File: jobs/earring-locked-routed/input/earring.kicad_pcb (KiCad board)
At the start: 4 copper layers, 30.5 x 35.8 mm, 167 parts, among them J1 USB-C, Q1 ALS-PT19, Q10 BSS138W, Q2 CJ2101, Q3 BSS138W, Q4 LBSS84WT1G, Q5 BSS138W, Q6 BSS138W, Q7 BSS138W, Q8 CJ2101, Q9 BSS138W, SW2 PWR, U1 RP2350A, U10 TPS22913, U2 LGS4056H, U3 NCP730-3.3, U4 TPS22913, U5 USBLC6-2P6, U6 LSM6DS3TR-C, U7 W25Q16JVUXIQ, U8 74LVC2G14, U9 TPS22913, Y1 12MHz

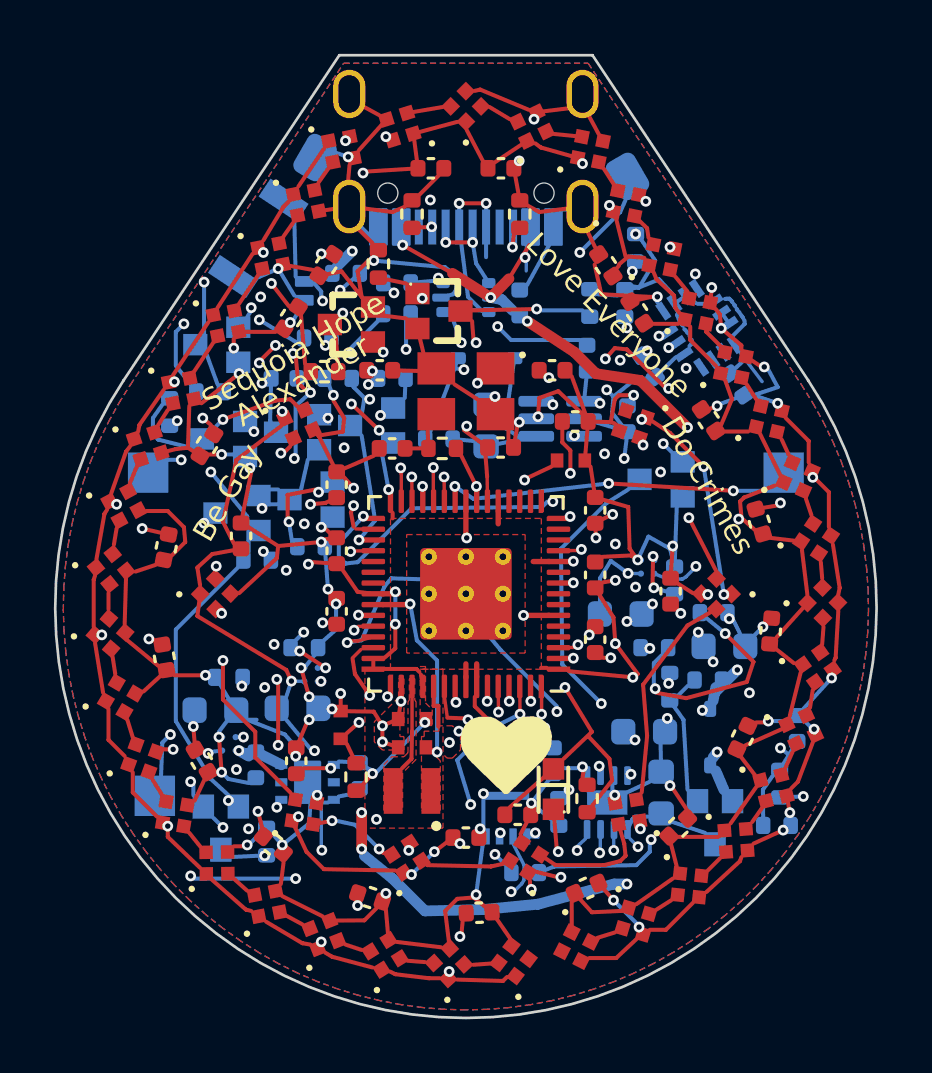
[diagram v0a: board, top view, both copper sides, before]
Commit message: Core: differential pairs routed coupled; both boards re-solved with their USB pairs
--diff-pairs finds pairs by net name (USB_DP/USB_DM, USB_C_DP/USB_C_DN, CLK_P/CLK_N, A+/A-),
takes a pad of each net close together as a pair's end, and routes each run between ends as one
centreline, wide enough for both tracks and the class's diff-pair gap, on a single layer; the
two tracks are laid along it and the router adds the pad legs. Runs go after the fine-pitch
escapes, so they block no pins, and are kept apart from copper the router may rip or pull.
The studio turns it on by default ("Route USB pairs side by side").

The cleanup cuts a track loose at both ends back to its outermost joints and cuts a tail back
to a joint already inside it, so no pair run is left dangling.

Re-solved (KiCad: 0 unconnected, 0 errors): earring-routed with USB_DP/DM 86%/78% coupled,
earring-locked-routed 92%/79%, bluebuzz-routed USB_DP/DM 81%/80% with 0.18 mm skew (the
hand-routed board: 31%). From bare pads, one thread: earring 5 of 6 seeds connected (was 4),
bluebuzz 6 of 6. examples/pair_check measures coupling.

Co-Authored-By: Claude Opus 5.5 (1M context) <noreply@anthropic.com>
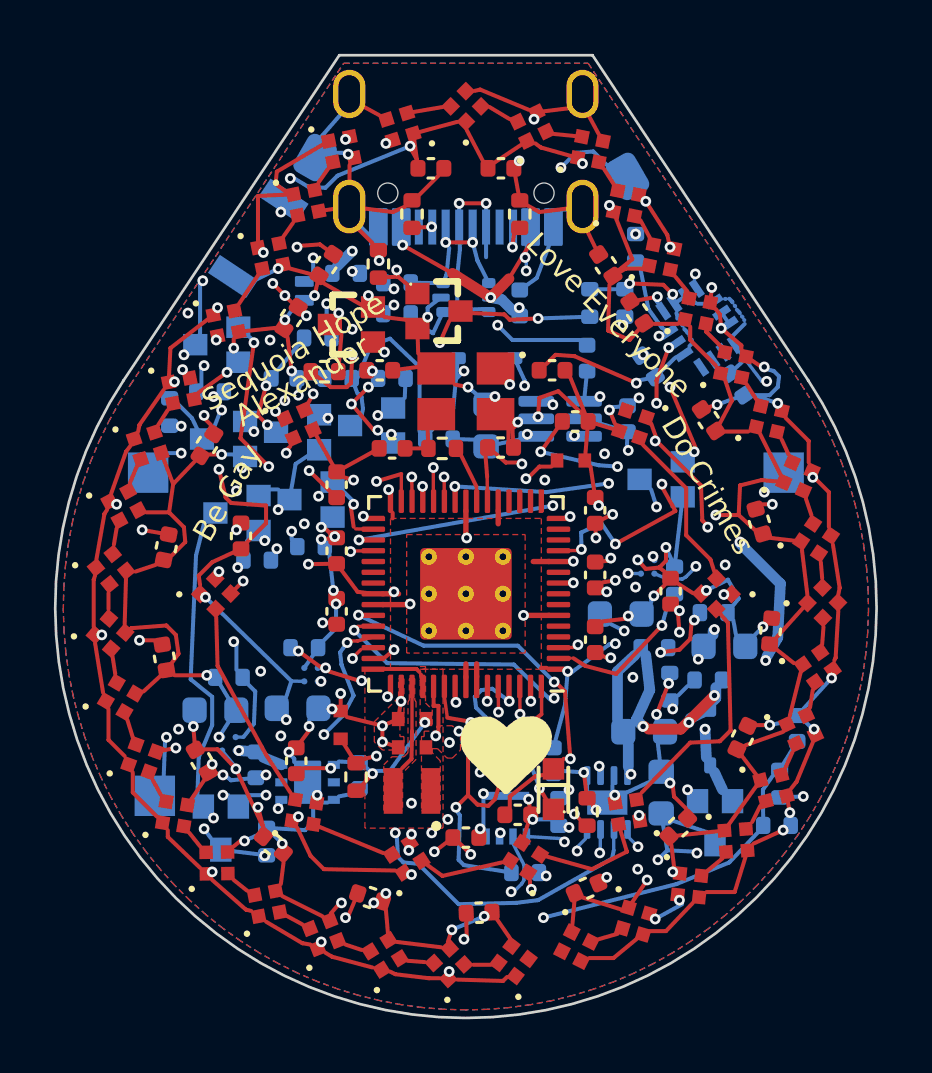
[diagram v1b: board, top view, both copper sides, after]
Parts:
- moved R16 0.50 mm to (104.5, 107.6)
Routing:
- net USB_DM: track 56.4 -> 23.1 mm
- net CHRG: track 42.1 -> 22.9 mm, vias 6 -> 4
- net RUN: track 38.8 -> 22.5 mm, vias 6 -> 4
- net USB_DP: track 35.1 -> 19.4 mm, vias 8 -> 3
- net BTN_SENSE: track 12.8 -> 28.2 mm
- net LED_EN_L: track 29.2 -> 43.8 mm, vias 6 -> 4
- net VBUS: track 41.4 -> 53.4 mm, vias 12 -> 13
- net VLED_L: track 57.7 -> 68.0 mm, vias 17 -> 21
- net PWR_EN: track 24.9 -> 32.5 mm, vias 9 -> 5
- net VLED_R: track 63.8 -> 70.6 mm, vias 6 -> 10
- net LONG: track 4.81 -> 11.4 mm, vias 2 -> 3
- net VBSENSE: track 43.6 -> 37.2 mm, vias 3 -> 4
- net VSYS: track 51.6 -> 46.8 mm, vias 10 -> 9
- net VBUS_SENSE: track 20.8 -> 15.9 mm, vias 3 -> 4
- net BTN_N: track 8.35 -> 3.57 mm
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
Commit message: Core: differential pairs length-matched, and the short pair coupled; jobs re-solved
Length matching (grid::match_lengths): after the cleanup each pair's nets are measured end to
end along their copper and the shorter one is given bumps, one at a time, the tallest that lays,
on uncoupled tracks first; a bump that does not reduce the skew is undone.

The short pair: pins of a pair whose ends share a layer are left out of the fan-out, a run's
layer is chosen by cost (length, a price per via its ends need, how far from the pins it
starts) with each layer trying its nearest start ring first, and pair runs may cross pours,
kept block planes included, to be refilled round them. bluebuzz's resistor-to-RP2350 pair now
runs side by side on F.Cu with no via.

Re-solved (KiCad: 0 unconnected, 0 errors, no part moved): earring-routed, pairs 0.00 and 0.16
mm apart; earring-locked-routed 0.00 and 0.00; bluebuzz-routed 0.00 (76%/72% side by side)
and 0.13 mm (58%/60%). job.json `args` gives the studio the seed each job routes best with.

Co-Authored-By: Claude Opus 5.5 (1M context) <noreply@anthropic.com>
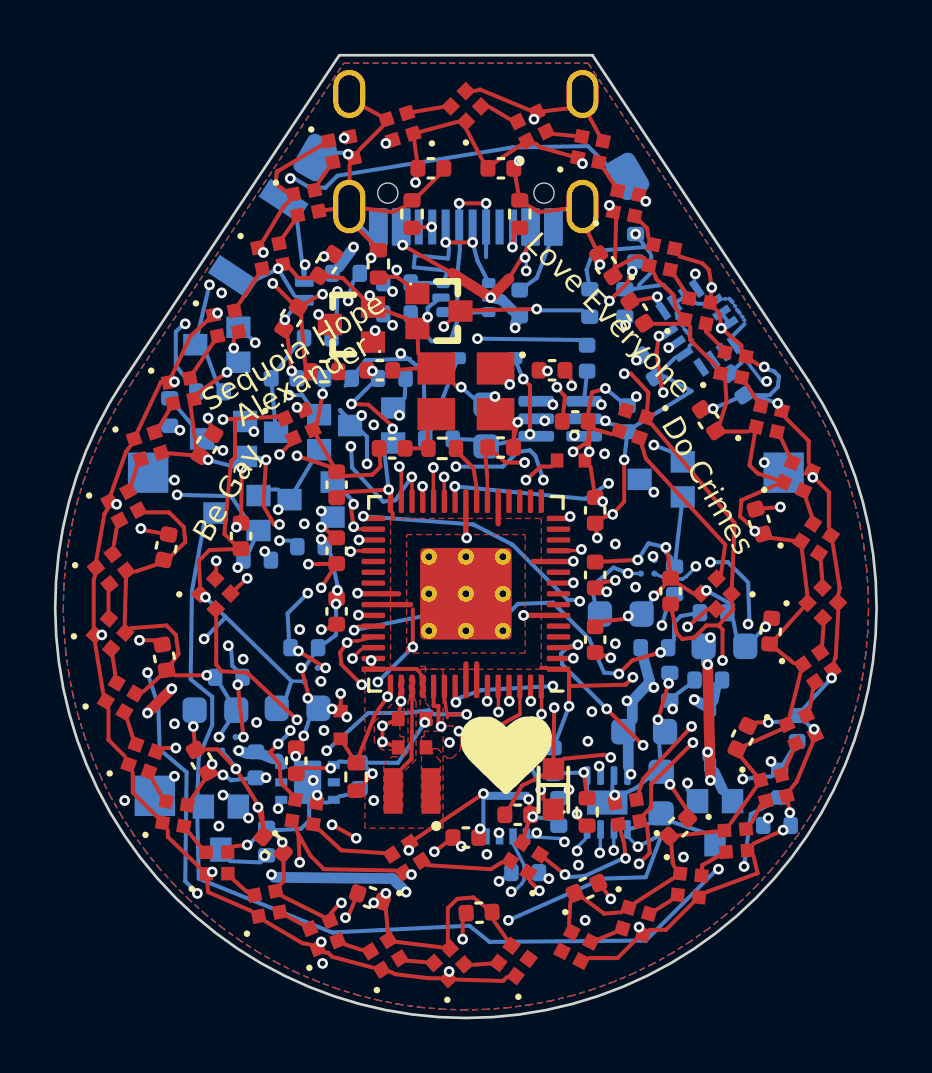
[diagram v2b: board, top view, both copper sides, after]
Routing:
- net PWR_EN: track 32.5 -> 66.9 mm, vias 5 -> 8
- net VLED_C: track 61.1 -> 75.8 mm, vias 18 -> 15
- net USB_DM: track 23.1 -> 34.6 mm, vias 3 -> 4
- net VBUS: track 53.4 -> 42.3 mm, vias 13 -> 11
- net VSYS: track 46.8 -> 56.7 mm, vias 9 -> 16
- net BTN_SENSE: track 28.2 -> 18.3 mm, vias 3 -> 4
- net LED_EN_L: track 43.8 -> 51.2 mm, vias 4 -> 10
- net VBATT: track 58.2 -> 65.6 mm
- net LONG: track 11.4 -> 4.35 mm, vias 3 -> 2
- net VBSENSE: track 37.2 -> 43.4 mm, vias 4 -> 6
- net LEDC_D6: track 8.92 -> 15.0 mm, vias 0 -> 4
- net USB_DP: track 19.4 -> 25.4 mm, vias 3 -> 4
- net BOOTSEL_SW: track 23.3 -> 17.7 mm
- net GND: track 208.9 -> 213.8 mm, vias 88 -> 91
- net VLED_L: track 68.0 -> 63.3 mm, vias 21 -> 19
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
